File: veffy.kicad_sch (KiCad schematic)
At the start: 56 parts, among them J1 SWD, Q2 BFR93A, SW1 SW_Push, U1 ATSAMD21G18A-A, U2 ADF4112BCPZ, U3 SA612AN/01_112, U4 MC3361, U5 LM386, U6 LM358_DFN, U7 AD9834

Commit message: initial DDS Modulator done!
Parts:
- added C30, C31, C32: 0.1uF, symbol Device:C
- added R12: R, symbol Device:R
- added R13: 6.8K, symbol Device:R
- added R14, R15: 200, symbol Device:R
- added Y1: Crystal, symbol Device:Crystal
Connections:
- net +3.3V: now also U7.11 (RESET), U7.4 (AVDD), U7.5 (DVDD), C31.1, C32.1, R12.1, R12.2
- net GND: now also U7.10 (PSELECT), U7.12 (SLEEP), U7.18 (AGND), U7.7 (DGND), U7.9 (FSELECT), C30.2, C31.2, C32.2, R13.2, R14.2, R15.2
- net MOSI: now also U7.13 (SDATA)
- net SCK: now also U7.14 (SCLK)
- net at U7.1 (FS_ADJUST): now also R13.1
- net FSYNC: now reaches U7.15 (~{FSYNC})
- net at U7.19 (IOUT): now also R14.1
- net at U7.20 (IOUTB): now also R15.1
- net at U7.3 (COMP): now also C30.1
- no-connect marks 11 -> 12
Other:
- note added: "DDS Modulator"
- moved on the sheet: U7

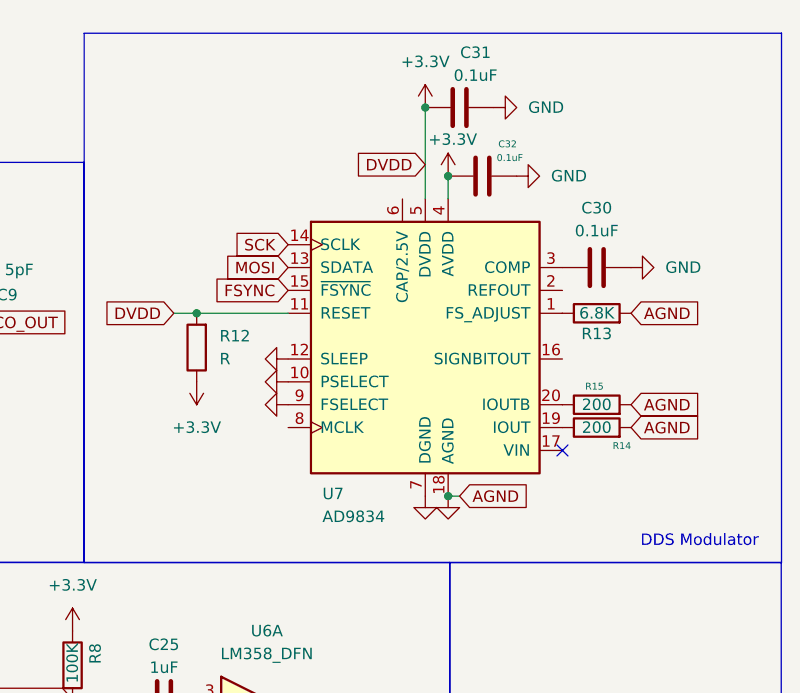
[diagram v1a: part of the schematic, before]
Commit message: fixed some issues with the DDS Modulator
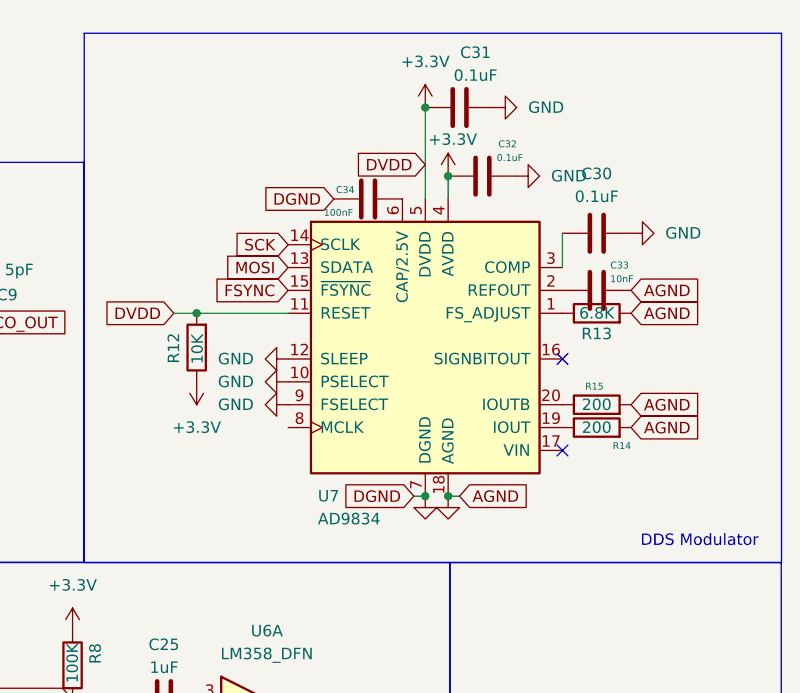
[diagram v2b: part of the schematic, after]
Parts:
- added C33: 10nF, symbol Device:C
- added C34: 100nF, symbol Device:C
- R12: value R -> 10K
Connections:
- net GND: now also C33.2, C34.2
- net at U7.2 (REFOUT): now also C33.1
- net at U7.6 (CAP/2.5V): now also C34.1
- no-connect marks 12 -> 13
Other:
- moved on the sheet: C30

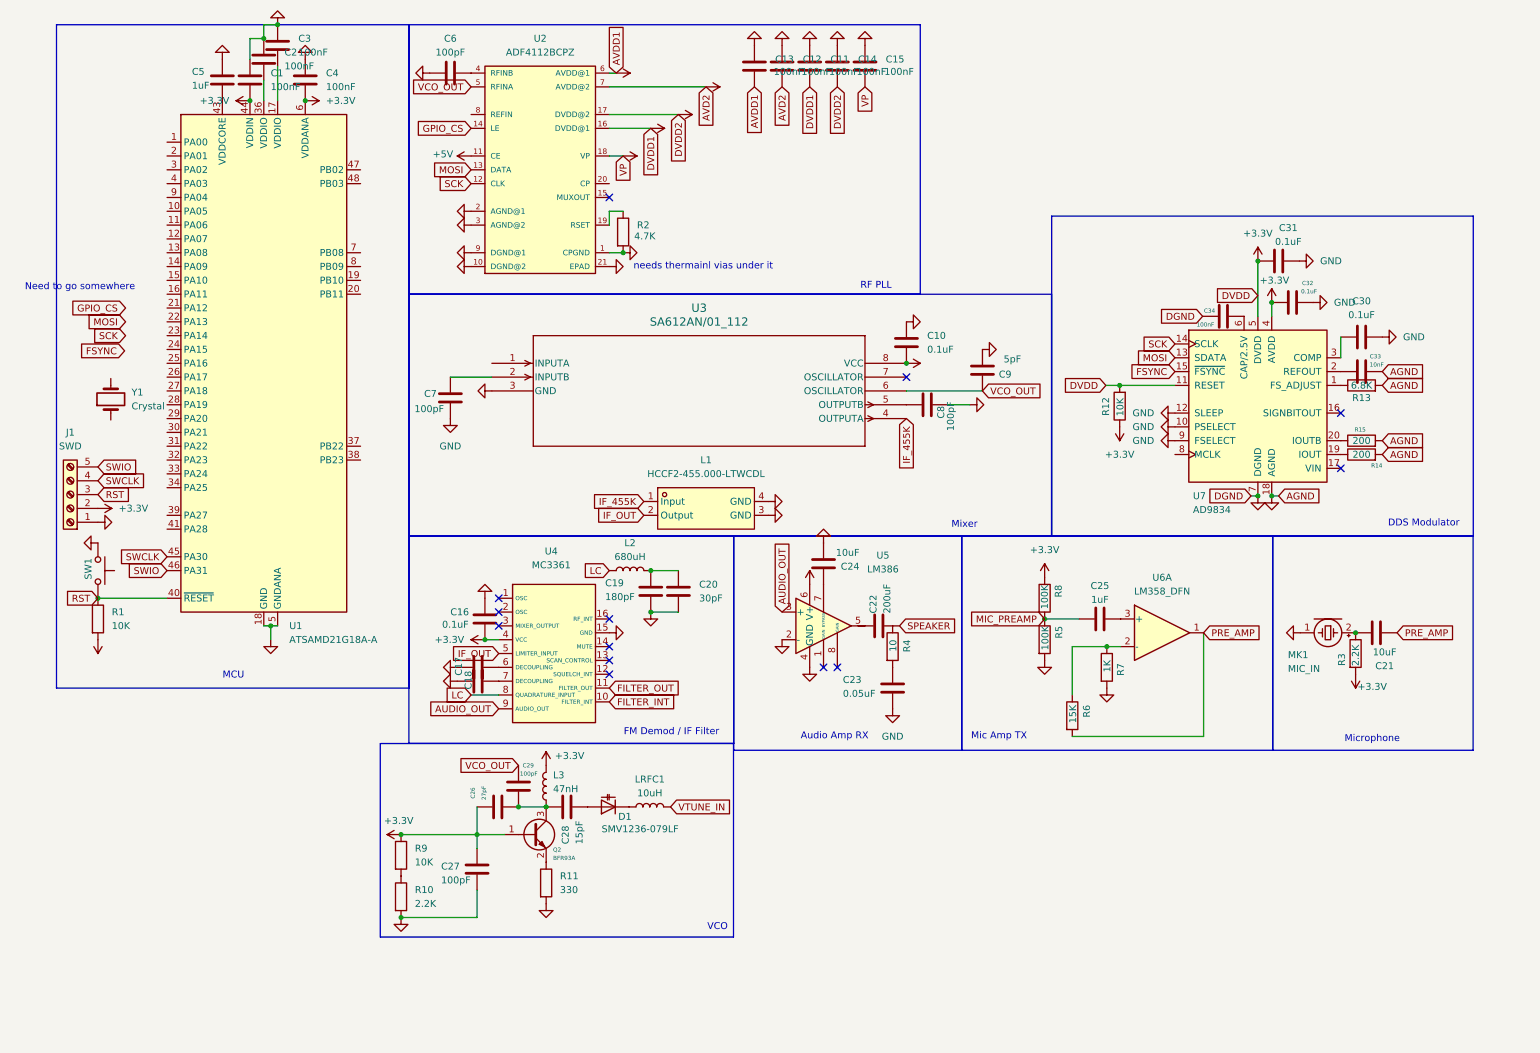
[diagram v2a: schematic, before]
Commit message: TCXO wiring is done
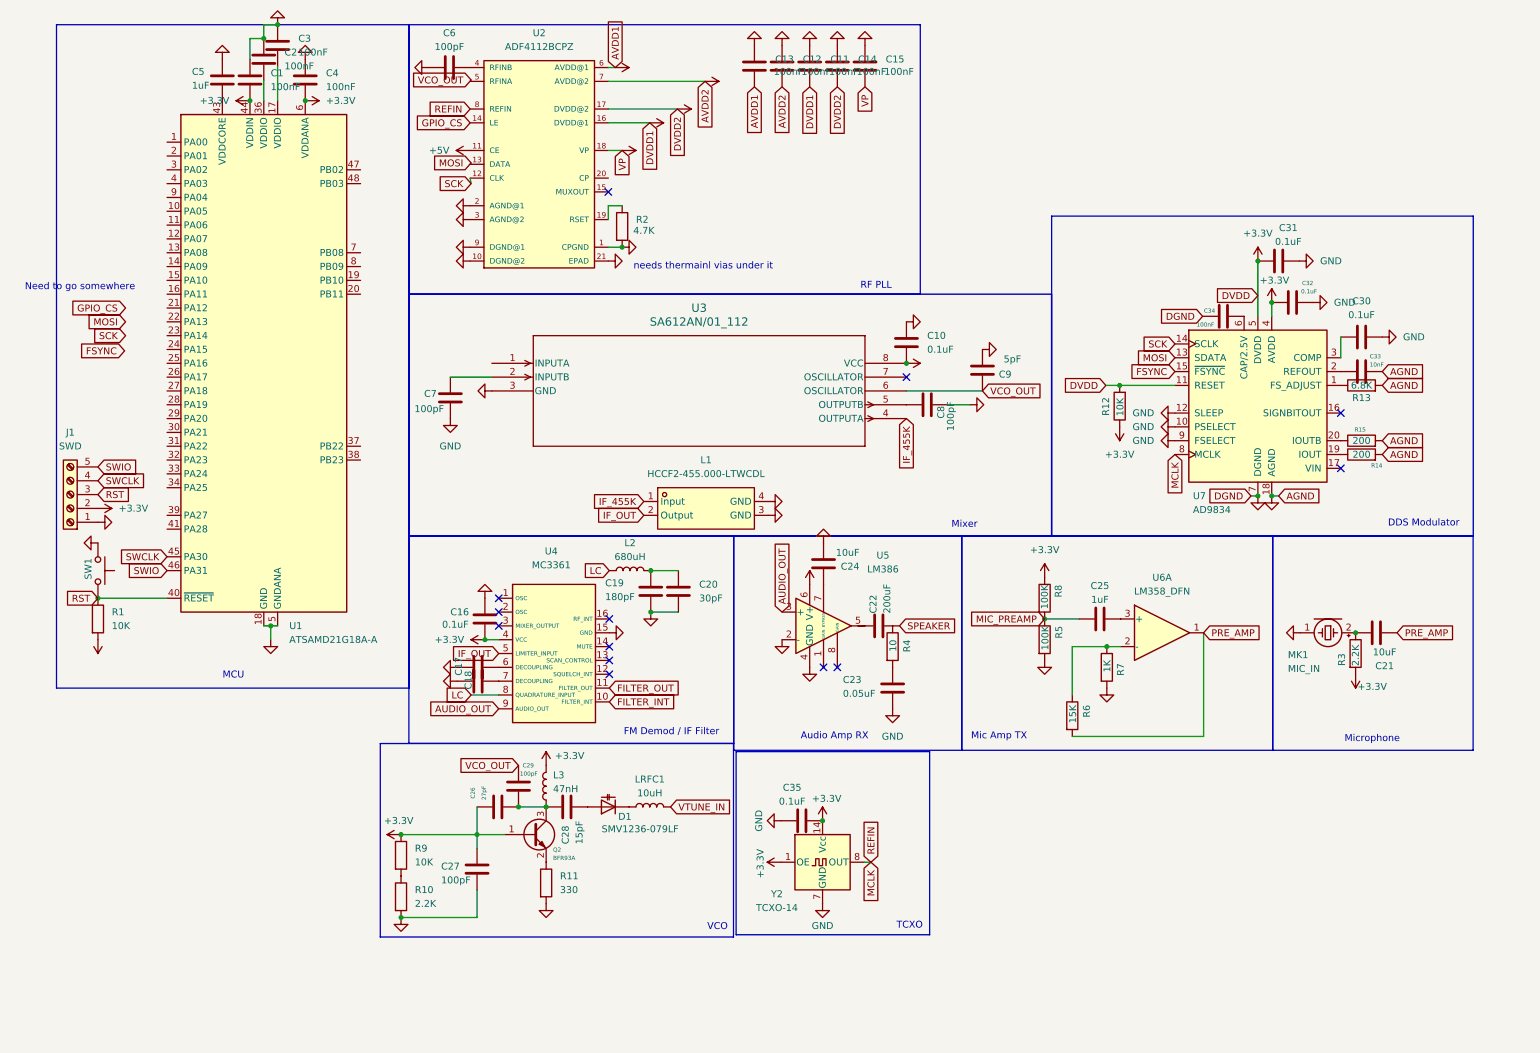
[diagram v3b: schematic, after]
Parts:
- removed Y1: Crystal, symbol Device:Crystal
- added C35: 0.1uF, symbol Device:C
- added Y2: TCXO-14, Oscillator:Oscillator_DIP-14, symbol Oscillator:CXO_DIP14
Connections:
- net +3.3V: now also C35.2, Y2.1 (OE), Y2.14 (Vcc)
- net GND: now also C35.1, Y2.7 (GND)
- net MCLK: now reaches U2.8 (REFIN)
- net MCLK: now also U7.8 (MCLK), Y2.8 (OUT)
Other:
- note added: "TCXO"
- moved on the sheet: C6, R2, U2

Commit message: T/R Switch almost done
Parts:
- added C36: 100pF, symbol Device:C
- added D2: BAR64-05W, Package_TO_SOT_SMD:SOT-323_SC-70, symbol Diode:BAT54CW
- added L4, L5: 100nH, symbol Device:L
- added L6: 1uH, symbol Device:L
- C1, C10, C11, C12, C13, C14, C15, C16, C17, C18, C19, C2, C20, C21, C22, C23, C24, C25, C3, C30, C31, C32, C33, C34, C35, C4, C5, C6, C7, C8, C9: footprint (none) -> Capacitor_SMD:C_0603_1608Metric_Pad1.08x0.95mm_HandSolder
- C26, C27, C28, C29: footprint NP0 -> Capacitor_SMD:C_0603_1608Metric_Pad1.08x0.95mm_HandSolder
- R1, R10, R11, R12, R13, R14, R15, R2, R3, R4, R5, R6, R7, R8, R9: footprint (none) -> Resistor_SMD:R_0603_1608Metric_Pad0.98x0.95mm_HandSolder
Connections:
- net +3.3V: now also L4.1, L5.1
- net GND: now also L6.2
- new net: C36.2, D2.3
- new net ANT: C36.1
- new net RX_MIX_INT: D2.1, L4.2
- new net TX_UPCNVRT_OUT: D2.2, L5.2
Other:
- note added: "T/R Switch"

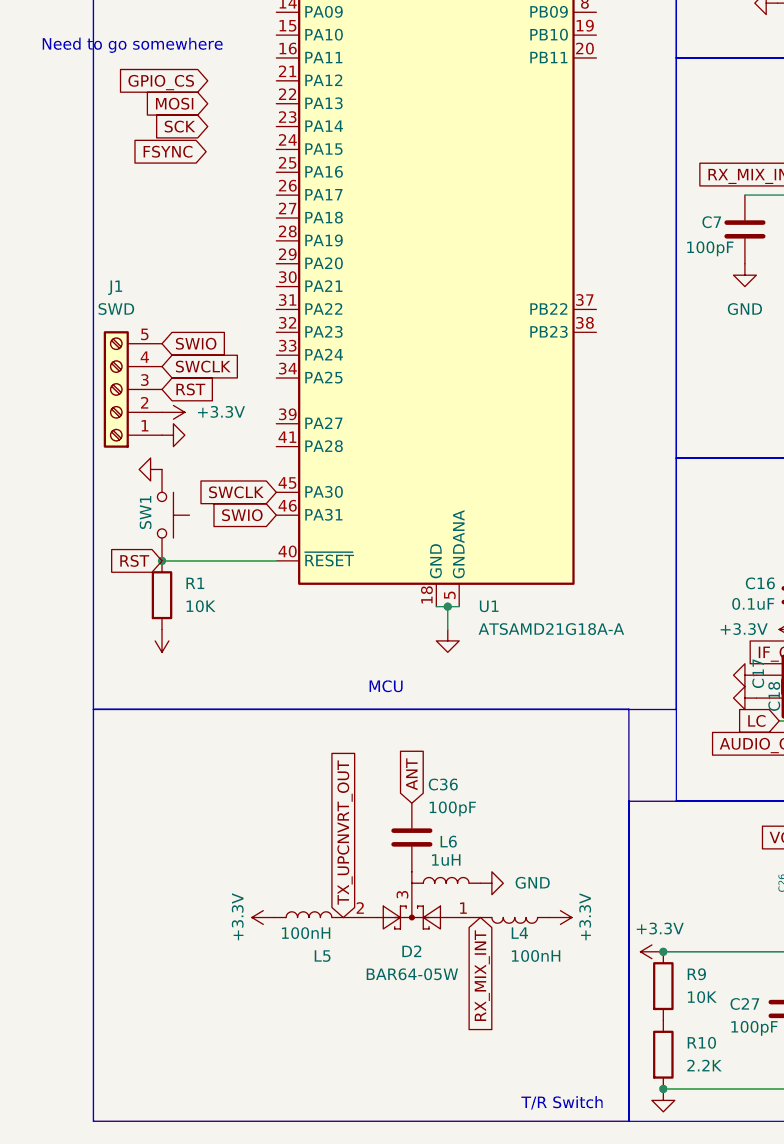
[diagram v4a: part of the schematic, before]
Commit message: T/R switch is finally fixed and finished!
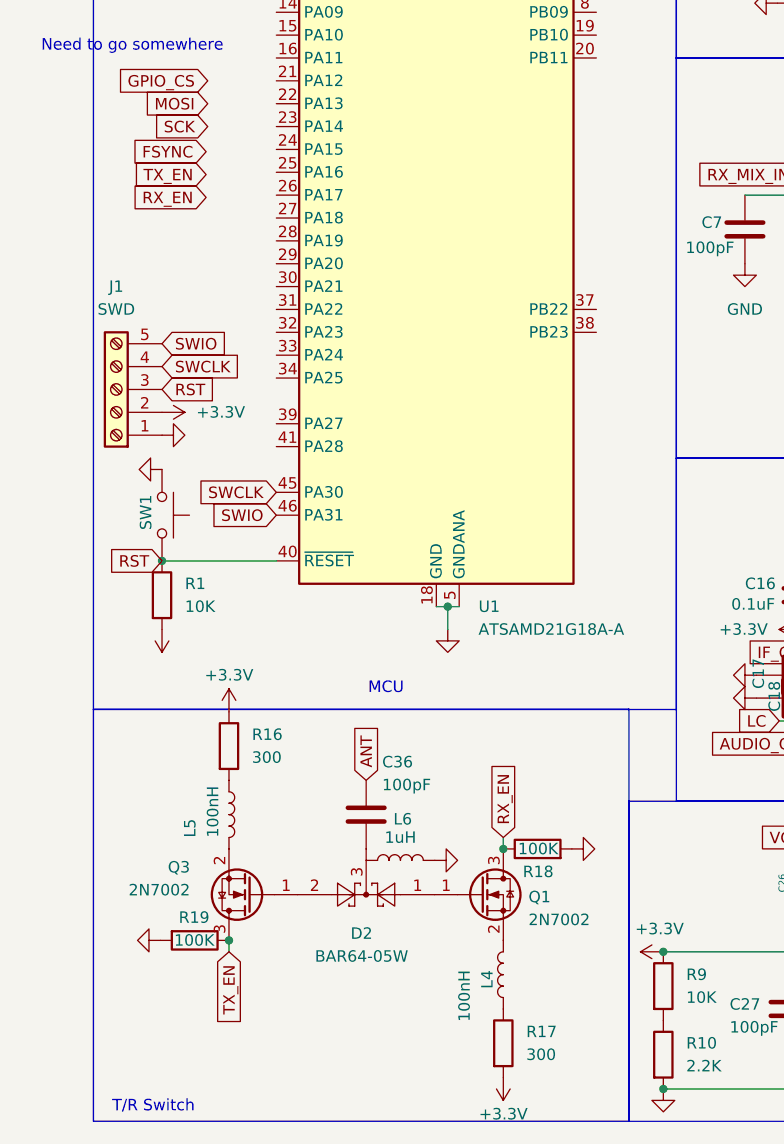
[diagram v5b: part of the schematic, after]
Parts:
- added Q1, Q3: 2N7002, Package_TO_SOT_SMD:SOT-23, symbol Transistor_FET:2N7002
- added R16, R17: 300, Resistor_SMD:R_0603_1608Metric_Pad0.98x0.95mm_HandSolder, symbol Device:R
- added R18, R19: 100K, Resistor_SMD:R_0603_1608Metric_Pad0.98x0.95mm_HandSolder, symbol Device:R
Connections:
- net +3.3V: now also R16.1, R17.2; no longer L4.1, L5.1
- net GND: now also R18.2, R19.2
- net RX_MIX_INT: no longer D2.1, L4.2
- net TX_UPCNVRT_OUT: no longer names the net of D2.2
- net TX_UPCNVRT_OUT: now also Q3.1 (G); no longer L5.2
- new net: L4.1, R17.1
- new net: D2.1, Q1.1 (G)
- new net: L4.2, Q1.2 (S)
- new net: L5.1, R16.2
- new net: L5.2, Q3.2 (S)
- new net RX_EN: Q1.3 (D), R18.1
- new net TX_EN: Q3.3 (D), R19.1
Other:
- moved on the sheet: C36, D2, L6
